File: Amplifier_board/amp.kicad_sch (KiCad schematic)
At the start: 24 parts, among them U4 TPA3111D1PWPR

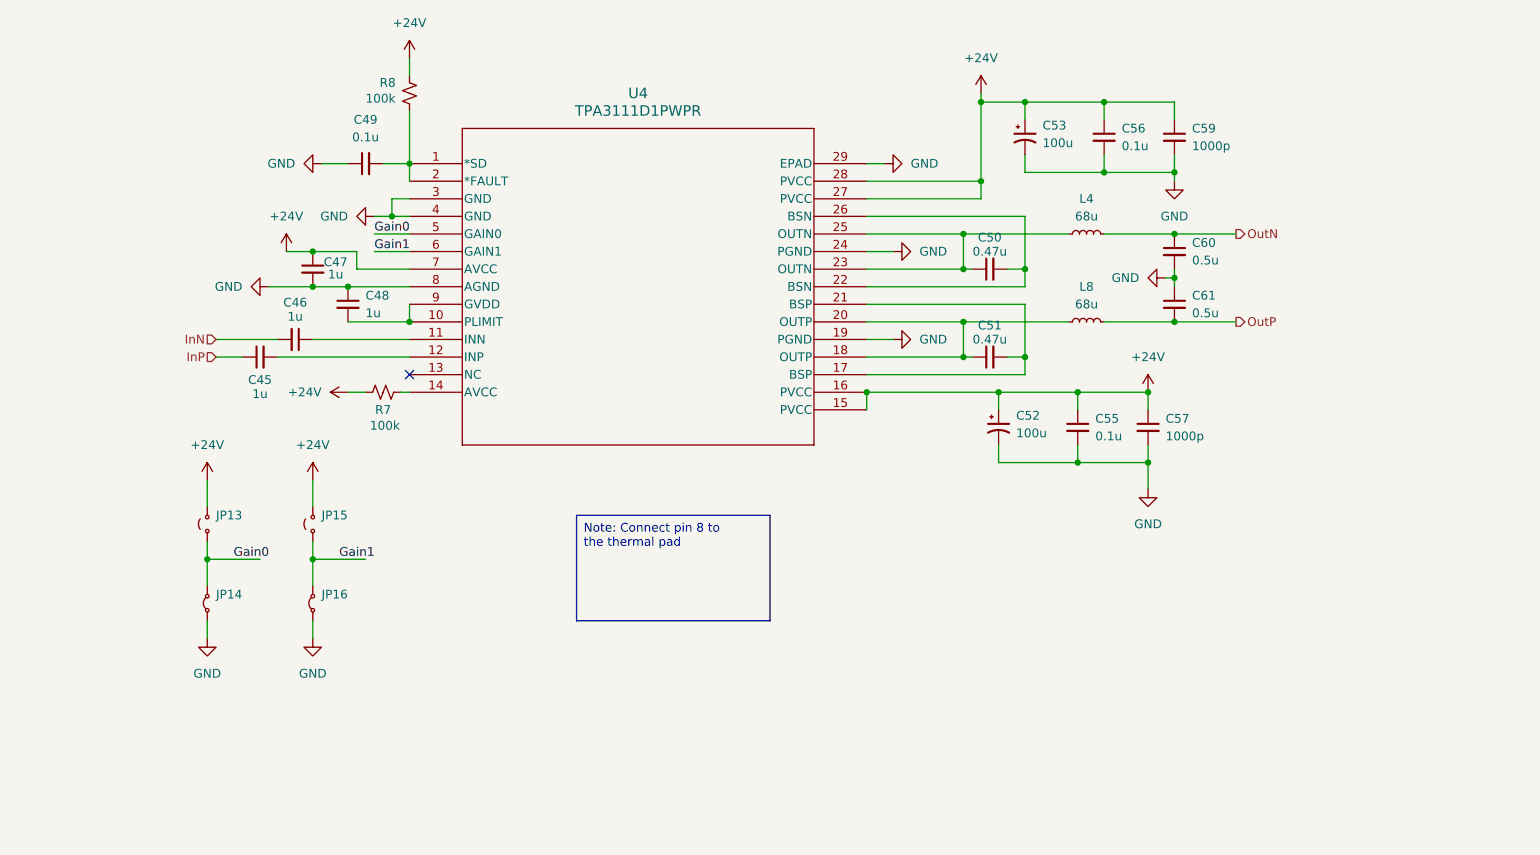
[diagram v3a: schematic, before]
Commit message: Started layout of amplifier board
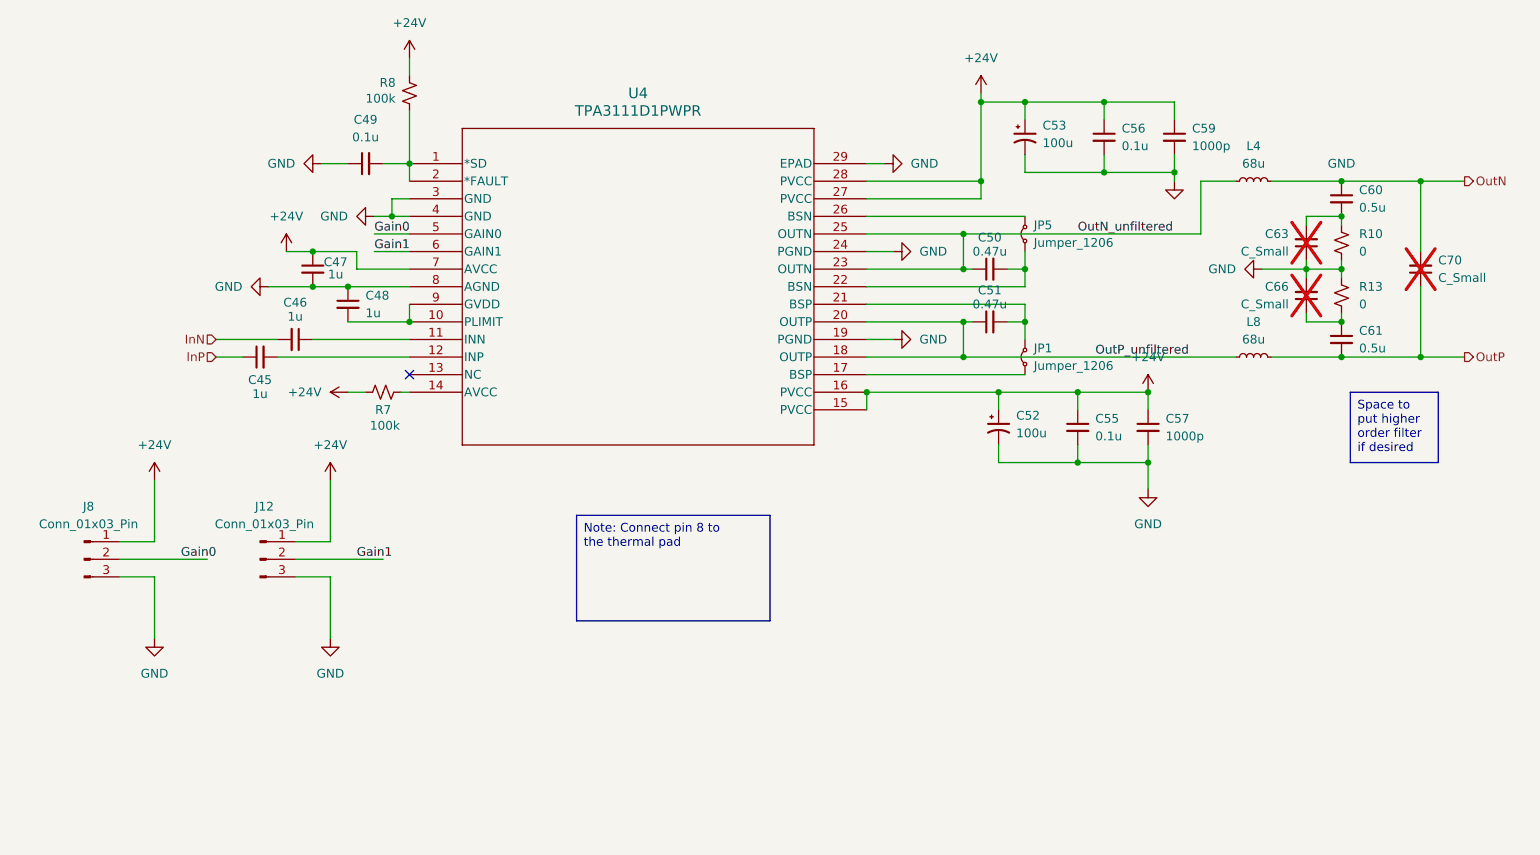
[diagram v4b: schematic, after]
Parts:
- removed JP13, JP15: Jumper_2_Small_Open, Jumper:SolderJumper-2_P1.3mm_Open_TrianglePad1.0x1.5mm, symbol Jumper:Jumper_2_Small_Open
- removed JP14, JP16: Jumper_2_Small_Bridged, Jumper:SolderJumper-2_P1.3mm_Open_TrianglePad1.0x1.5mm, symbol Jumper:Jumper_2_Small_Bridged
- added C63, C66, C70: C_Small, Capacitor_SMD:C_0805_2012Metric_Pad1.18x1.45mm_HandSolder, symbol Device:C_Small
- added J12, J8: Conn_01x03_Pin, Connector_PinSocket_2.54mm:PinSocket_1x03_P2.54mm_Vertical, symbol Connector:Conn_01x03_Pin
- added JP1, JP5: Jumper_1206, Resistor_SMD:R_1206_3216Metric_Pad1.30x1.75mm_HandSolder, symbol Jumper:Jumper_2_Small_Bridged
- added R10, R13: 0, Resistor_SMD:R_0805_2012Metric_Pad1.20x1.40mm_HandSolder, symbol Device:R_Small_US
- C52, C53: footprint Capacitor_SMD:C_0805_2012Metric_Pad1.18x1.45mm_HandSolder -> project_lib:WCAP-ASLI_6.3X7.7_DXL_
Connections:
- net +24V: now also J12.1 (Pin_1), J8.1 (Pin_1)
- net GND: now also C63.1, C66.2, J12.3 (Pin_3), J8.3 (Pin_3), R10.1, R13.2; no longer C60.2, C61.1
- net Gain0: now also J8.2 (Pin_2)
- net Gain1: now also J12.2 (Pin_2)
- net OutN: now also C70.2
- net OutP: now also C70.1
- net OutN_unfiltered: now reaches C50.1, L4.1, U4.23 (OUTN), U4.25 (OUTN)
- net at C50.2, U4.22 (BSN): now also JP5.1 (A); no longer U4.26 (BSN)
- net OutP_unfiltered: now reaches C51.1, L8.1, U4.18 (OUTP), U4.20 (OUTP)
- net at C51.2, U4.21 (BSP): now also JP1.2 (B); no longer U4.17 (BSP)
- new net: JP1.1 (A), U4.17 (BSP)
- new net: C61.1, C66.1, R13.1
- new net: C60.2, C63.2, R10.2
- new net: JP5.2 (B), U4.26 (BSN)
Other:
- moved on the sheet: C51, C60, C61, L4, L8

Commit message: More progress on layout
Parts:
- C60, C61: value 0.5u -> 0.47u
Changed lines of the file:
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@@
 			)
 		)
-		(property "Value" "0.5u"
+		(property "Value" "0.47u"
 			(at 240.03 69.8562 0)
 			(effects
@@
 			)
 		)
-		(property "Value" "0.5u"
+		(property "Value" "0.47u"
 			(at 240.03 90.1762 0)
 			(effects

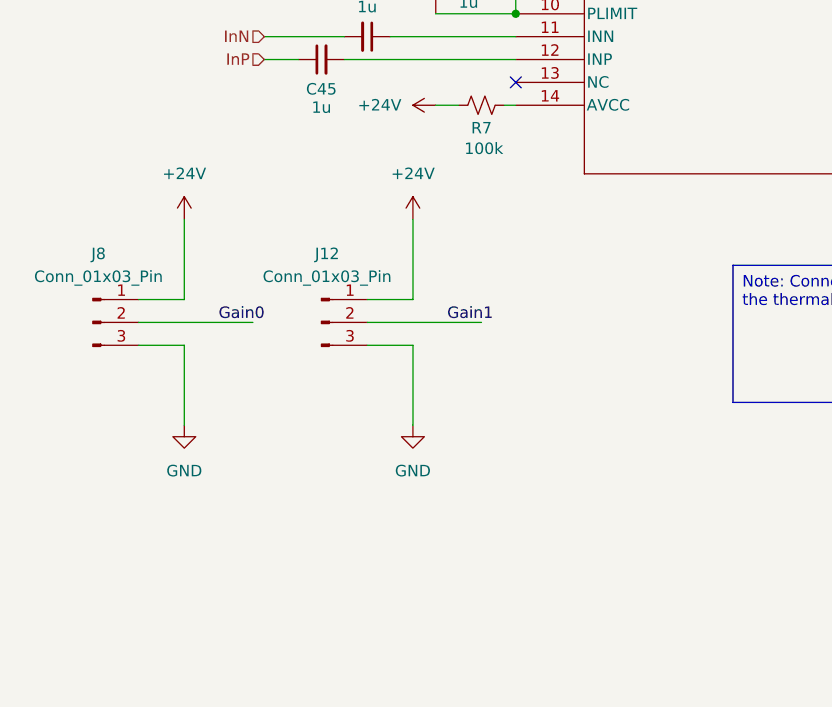
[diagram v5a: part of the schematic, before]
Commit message: More routing on amp board
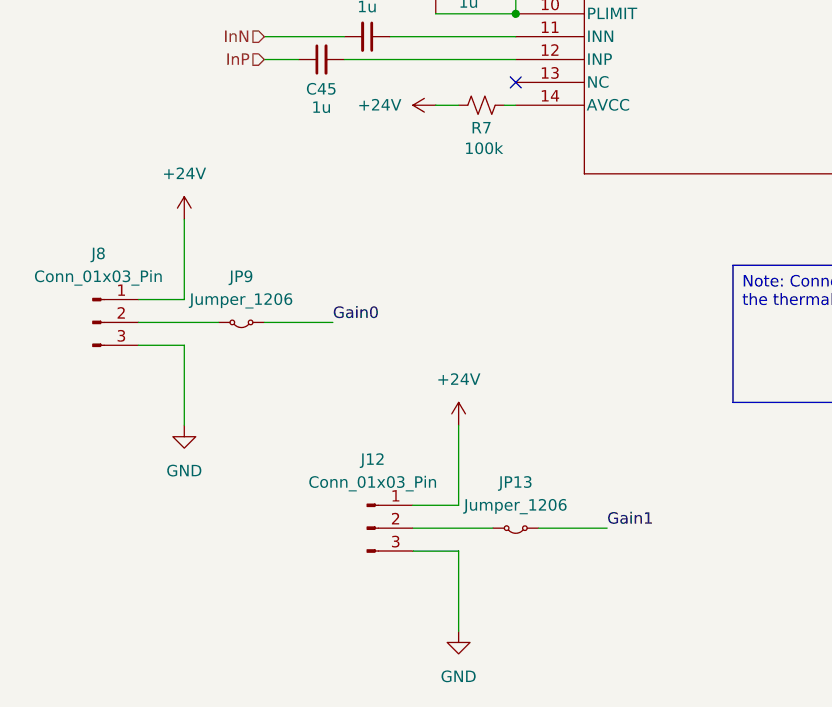
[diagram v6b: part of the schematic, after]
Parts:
- added JP13, JP9: Jumper_1206, Resistor_SMD:R_1206_3216Metric_Pad1.30x1.75mm_HandSolder, symbol Jumper:Jumper_2_Small_Bridged
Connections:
- net Gain0: now also JP9.1 (A); no longer J8.2 (Pin_2)
- net Gain1: now also JP13.1 (A); no longer J12.2 (Pin_2)
- new net: J8.2 (Pin_2), JP9.2 (B)
- new net: J12.2 (Pin_2), JP13.2 (B)
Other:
- moved on the sheet: J12
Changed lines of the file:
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@@
 	(wire
 		(pts
-			(xy 60.96 120.65) (xy 73.66 120.65)
+			(xy 168.91 88.9) (xy 172.72 88.9)
 		)
 		(stroke
@@
 	(wire
 		(pts
-			(xy 86.36 120.65) (xy 99.06 120.65)
+			(xy 60.96 120.65) (xy 69.85 120.65)
 		)
 		(stroke
@@
 	(wire
 		(pts
-			(xy 168.91 88.9) (xy 172.72 88.9)
+			(xy 91.44 143.51) (xy 100.33 143.51)
 		)
 		(stroke
@@
 	(wire
 		(pts
-			(xy 86.36 123.19) (xy 91.44 123.19)
+			(xy 91.44 146.05) (xy 96.52 146.05)
 		)
 		(stroke
@@
 	(wire
 		(pts
-			(xy 91.44 118.11) (xy 86.36 118.11)
+			(xy 96.52 140.97) (xy 91.44 140.97)
 		)
 		(stroke
@@
 	(wire
 		(pts
-			(xy 91.44 109.22) (xy 91.44 118.11)
+			(xy 96.52 132.08) (xy 96.52 140.97)
 		)
 		(stroke
@@
 	(wire
 		(pts
+			(xy 74.93 120.65) (xy 82.55 120.65)
+		)
+		(stroke
+			(width 0)
+			(type default)
+		)
+	)
+	(wire
+		(pts
 			(xy 100.33 68.58) (xy 100.33 71.12)
 		)
@@
 	(wire
 		(pts
-			(xy 91.44 123.19) (xy 91.44 132.08)
+			(xy 96.52 146.05) (xy 96.52 154.94)
 		)
 		(stroke
@@
 	(wire
 		(pts
+			(xy 105.41 143.51) (xy 113.03 143.51)
+		)
+		(stroke
+			(width 0)
+			(type default)
+		)
+	)
+	(wire
+		(pts
 			(xy 168.91 63.5) (xy 171.45 63.5)
 		)
@@
 		)
 	)
-	(label "Gain1"
-		(at 95.25 120.65 0)
+	(label "Gain0"
+		(at 97.79 73.66 0)
 		(fields_autoplaced yes)
 		(effects
@@
 		)
 	)
-	(label "Gain0"
-		(at 97.79 73.66 0)
+	(label "OutP_unfiltered"
+		(at 201.93 91.44 0)
 		(fields_autoplaced yes)
 		(effects
@@
 		)
 	)
-	(label "OutP_unfiltered"
-		(at 201.93 91.44 0)
+	(label "Gain0"
+		(at 82.55 120.65 0)
 		(fields_autoplaced yes)
 		(effects
@@
 		)
 	)
-	(label "Gain0"
-		(at 69.85 120.65 0)
+	(label "Gain1"
+		(at 113.03 143.51 0)
 		(fields_autoplaced yes)
 		(effects
@@
 	(symbol
 		(lib_id "power:+24V")
-		(at 91.44 109.22 0)
+		(at 96.52 132.08 0)
 		(unit 1)
 		(exclude_from_sim no)
@@
 		(fields_autoplaced yes)
 		(property "Reference" "#PWR060"
-			(at 91.44 113.03 0)
+			(at 96.52 135.89 0)
 			(effects
 				(font
@@
 		)
 		(property "Value" "+24V"
-			(at 91.44 104.14 0)
+			(at 96.52 127 0)
 			(effects
 				(font
@@
 		)
 		(property "Footprint" ""
-			(at 91.44 109.22 0)
+			(at 96.52 132.08 0)
 			(effects
 				(font
@@
 		)
 		(property "Datasheet" ""
-			(at 91.44 109.22 0)
+			(at 96.52 132.08 0)
 			(effects
 				(font
@@
 		)
 		(property "Description" "Power symbol creates a global label with name \"+24V\""
-			(at 91.44 109.22 0)
+			(at 96.52 132.08 0)
 			(effects
 				(font
@@
 	(symbol
 		(lib_id "Connector:Conn_01x03_Pin")
-		(at 81.28 120.65 0)
+		(at 86.36 143.51 0)
 		(unit 1)
 		(exclude_from_sim no)
@@
 		(fields_autoplaced yes)
 		(property "Reference" "J12"
-			(at 81.915 113.03 0)
+			(at 86.995 135.89 0)
 			(effects
 				(font
@@
 		)
 		(property "Value" "Conn_01x03_Pin"
-			(at 81.915 115.57 0)
+			(at 86.995 138.43 0)
 			(effects
 				(font
@@
 		)
 		(property "Footprint" "Connector_PinSocket_2.54mm:PinSocket_1x03_P2.54mm_Vertical"
-			(at 81.28 120.65 0)
+			(at 86.36 143.51 0)
 			(effects
 				(font
@@
 		)
 		(property "Datasheet" "~"
-			(at 81.28 120.65 0)
+			(at 86.36 143.51 0)
 			(effects
 				(font
@@
 		)
 		(property "Description" "Generic connector, single row, 01x03, script generated"
-			(at 81.28 120.65 0)
+			(at 86.36 143.51 0)
 			(effects
 				(font
@@
 	(symbol
 		(lib_id "power:GND")
-		(at 91.44 132.08 0)
+		(at 96.52 154.94 0)
 		(unit 1)
 		(exclude_from_sim no)
@@
 		(fields_autoplaced yes)
 		(property "Reference" "#PWR061"
-			(at 91.44 138.43 0)
+			(at 96.52 161.29 0)
 			(effects
 				(font
@@
 		)
 		(property "Value" "GND"
-			(at 91.44 137.16 0)
+			(at 96.52 160.02 0)
 			(effects
 				(font
@@
 		)
 		(property "Footprint" ""
-			(at 91.44 132.08 0)
+			(at 96.52 154.94 0)
 			(effects
 				(font
@@
 		)
 		(property "Datasheet" ""
-			(at 91.44 132.08 0)
+			(at 96.52 154.94 0)
 			(effects
 				(font
@@
 		)
 		(property "Description" "Power symbol creates a global label with name \"GND\" , ground"
-			(at 91.44 132.08 0)
+			(at 96.52 154.94 0)
 			(effects
 				(font
@@
 					(unit 1)
 				)
+			)
+		)
+	)
+	(symbol
+		(lib_id "Jumper:Jumper_2_Small_Bridged")
+		(at 102.87 143.51 180)
+		(unit 1)
+		(exclude_from_sim yes)
+		(in_bom yes)
+		(on_board yes)
+		(dnp no)
+		(fields_autoplaced yes)
+		(property "Reference" "JP13"
+			(at 102.87 138.43 0)
+			(effects
+				(font
+					(size 1.27 1.27)
+				)
+			)
+		)
+		(property "Value" "Jumper_1206"
+			(at 102.87 140.97 0)
+			(effects
+				(font
+					(size 1.27 1.27)
+				)
+			)
+		)
+		(property "Footprint" "Resistor_SMD:R_1206_3216Metric_Pad1.30x1.75mm_HandSolder"
+			(at 102.87 143.51 0)
+			(effects
+				(font
+					(size 1.27 1.27)
+				)
+				(hide yes)
+			)
+		)
+		(property "Datasheet" "~"
+			(at 102.87 143.51 0)
+			(effects
+				(font
+					(size 1.27 1.27)
+				)
+				(hide yes)
+			)
+		)
+		(property "Description" "Jumper, 2-pole, small symbol, bridged"
+			(at 102.87 143.51 0)
+			(effects
+				(font
+					(size 1.27 1.27)
+				)
+				(hide yes)
+			)
+		)
+		(pin "2"
+		)
+		(pin "1"
+		)
+		(instances
+			(project "Amplifier_board"
+				(path "/991395a4-3885-4774-b551-0bfe029123d3/1a21d9eb-2329-48b7-8877-ba841ad5b065"
+					(reference "JP16")
+					(unit 1)
+				)
+				(path "/991395a4-3885-4774-b551-0bfe029123d3/26541e86-2f42-461f-bb67-92277cc28a80"
+					(reference "JP13")
+					(unit 1)
+				)
+				(path "/991395a4-3885-4774-b551-0bfe029123d3/e8898fe0-55dc-4973-83e9-f265cc01a132"
+					(reference "JP15")
+					(unit 1)
+				)
+				(path "/991395a4-3885-4774-b551-0bfe029123d3/eadc8ba5-6d36-4b46-a20f-2896249de991"
+					(reference "JP14")
+					(unit 1)
+				)
+			)
+		)
+	)
+	(symbol
+		(lib_id "Jumper:Jumper_2_Small_Bridged")
+		(at 72.39 120.65 180)
+		(unit 1)
+		(exclude_from_sim yes)
+		(in_bom yes)
+		(on_board yes)
+		(dnp no)
+		(fields_autoplaced yes)
+		(property "Reference" "JP9"
+			(at 72.39 115.57 0)
+			(effects
+				(font
+					(size 1.27 1.27)
+				)
+			)
+		)
+		(property "Value" "Jumper_1206"
+			(at 72.39 118.11 0)
+			(effects
+				(font
+					(size 1.27 1.27)
+				)
+			)
+		)
+		(property "Footprint" "Resistor_SMD:R_1206_3216Metric_Pad1.30x1.75mm_HandSolder"
+			(at 72.39 120.65 0)
+			(effects
+				(font
+					(size 1.27 1.27)
+				)
+				(hide yes)
+			)
+		)
+		(property "Datasheet" "~"
+			(at 72.39 120.65 0)
+			(effects
+				(font
+					(size 1.27 1.27)
+				)
+				(hide yes)
+			)
+		)
+		(property "Description" "Jumper, 2-pole, small symbol, bridged"
+			(at 72.39 120.65 0)
+			(effects
+				(font
+					(size 1.27 1.27)
+				)
+				(hide yes)
+			)
+		)
+		(pin "2"
+		)
+		(pin "1"
+		)
+		(instances
+			(project "Amplifier_board"
+				(path "/991395a4-3885-4774-b551-0bfe029123d3/1a21d9eb-2329-48b7-8877-ba841ad5b065"
+					(reference "JP12")
+					(unit 1)
+				)
+				(path "/991395a4-3885-4774-b551-0bfe029123d3/26541e86-2f42-461f-bb67-92277cc28a80"
+					(reference "JP9")
+					(unit 1)
+				)
+				(path "/991395a4-3885-4774-b551-0bfe029123d3/e8898fe0-55dc-4973-83e9-f265cc01a132"
+					(reference "JP11")
+					(unit 1)
+				)
+				(path "/991395a4-3885-4774-b551-0bfe029123d3/eadc8ba5-6d36-4b46-a20f-2896249de991"
+					(reference "JP10")
+					(unit 1)
+				)
